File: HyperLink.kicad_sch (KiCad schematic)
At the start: 45 parts, among them J1 USB_C_Receptacle_USB2.0, J2 Conn_02x05_Odd_Even, J3 Conn_02x05_Odd_Even, SW1 SW_Push, U1 ESP32-C3, U2 PESD2USB5UXT, U3 MIC5504-3.3YM5, Y1 ABM11W-40.0000MHZ-8-B1U-T3

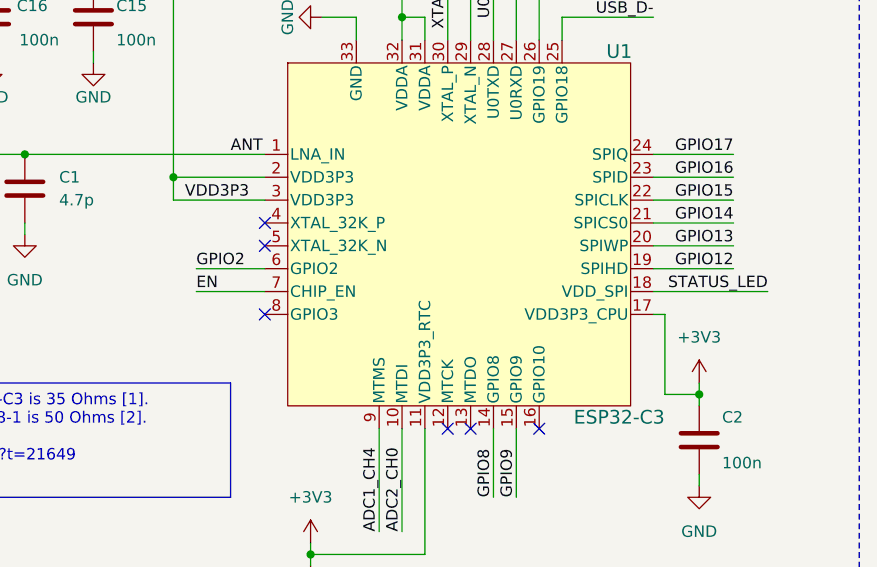
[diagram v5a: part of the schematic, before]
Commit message: Move status LED
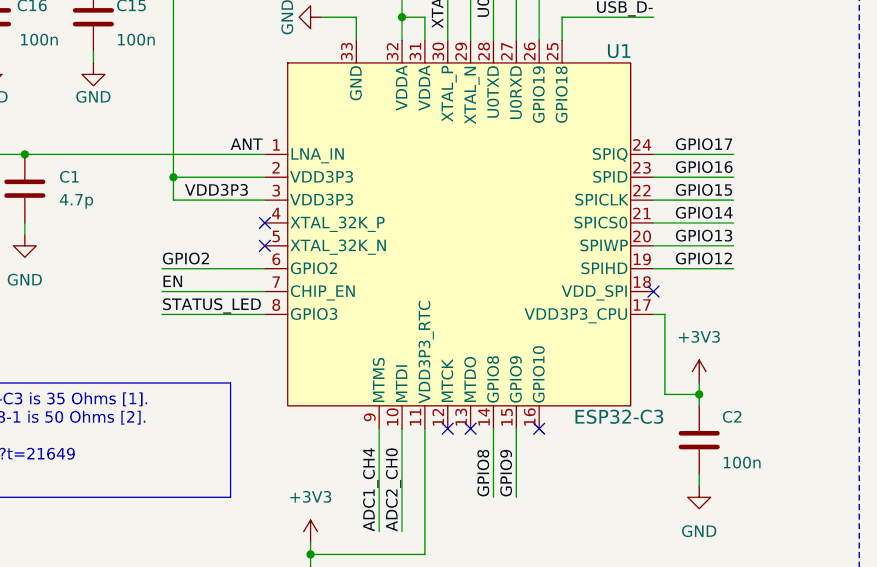
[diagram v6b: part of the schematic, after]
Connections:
- net STATUS_LED: now also U1.8 (GPIO3); no longer U1.18 (VDD_SPI)
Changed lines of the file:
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@@
   )
   (no_connect (at 241.3 116.84))
-  (no_connect (at 210.82 104.14))
   (no_connect (at 210.82 93.98))
   (no_connect (at 52.07 143.51))
   (no_connect (at 231.14 116.84))
+  (no_connect (at 254 101.6))
   (no_connect (at 52.07 146.05))
   (no_connect (at 233.68 116.84))
@@
     (stroke (width 0) (type default))
   )
-  (wire (pts (xy 203.2 99.06) (xy 210.82 99.06))
+  (wire (pts (xy 199.39 99.06) (xy 210.82 99.06))
     (stroke (width 0) (type default))
   )
@@
     (stroke (width 0) (type default))
   )
-  (wire (pts (xy 203.2 101.6) (xy 210.82 101.6))
+  (wire (pts (xy 199.39 101.6) (xy 210.82 101.6))
     (stroke (width 0) (type default))
   )
@@
     (stroke (width 0) (type default))
   )
+  (wire (pts (xy 199.39 104.14) (xy 210.82 104.14))
+    (stroke (width 0) (type default))
+  )
   (wire (pts (xy 160.02 86.36) (xy 166.37 86.36))
-    (stroke (width 0) (type default))
-  )
-  (wire (pts (xy 254 101.6) (xy 266.7 101.6))
     (stroke (width 0) (type default))
   )
@@
     (effects (font (size 1.27 1.27)) (justify left bottom))
   )
-  (label "EN" (at 203.2 101.6 0) (fields_autoplaced)
+  (label "EN" (at 199.39 101.6 0) (fields_autoplaced)
     (effects (font (size 1.27 1.27)) (justify left bottom))
   )
@@
     (effects (font (size 1.27 1.27)) (justify right bottom))
   )
+  (label "STATUS_LED" (at 199.39 104.14 0) (fields_autoplaced)
+    (effects (font (size 1.27 1.27)) (justify left bottom))
+  )
   (label "GPIO9" (at 238.76 124.46 90) (fields_autoplaced)
     (effects (font (size 1.27 1.27)) (justify left bottom))
   )
-  (label "STATUS_LED" (at 266.7 101.6 180) (fields_autoplaced)
-    (effects (font (size 1.27 1.27)) (justify right bottom))
-  )
   (label "GPIO17" (at 262.89 86.36 180) (fields_autoplaced)
     (effects (font (size 1.27 1.27)) (justify right bottom))
@@
     (effects (font (size 1.27 1.27)) (justify right bottom))
   )
-  (label "GPIO2" (at 203.2 99.06 0) (fields_autoplaced)
-    (effects (font (size 1.27 1.27)) (justify left bottom))
-  )
+  (label "GPIO2" (at 199.39 99.06 0) (fields_autoplaced)
+    (effects (font (size 1.27 1.27)) (justify left bottom))
+  )

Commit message: Check out new version of library and replace usb connector footprint
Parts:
- J1: footprint Connector_USB:USB_C_Receptacle_GCT_USB4105-xx-A_16P_TopMnt_Horizontal -> encyclopedia_galactica:USB4105-GF-A
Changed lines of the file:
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@@
       (effects (font (size 1.27 1.27)))
     )
-    (property "Footprint" "Connector_USB:USB_C_Receptacle_GCT_USB4105-xx-A_16P_TopMnt_Horizontal" (at 40.64 130.81 0)
+    (property "Footprint" "encyclopedia_galactica:USB4105-GF-A" (at 40.64 130.81 0)
       (effects (font (size 1.27 1.27)) hide)
     )

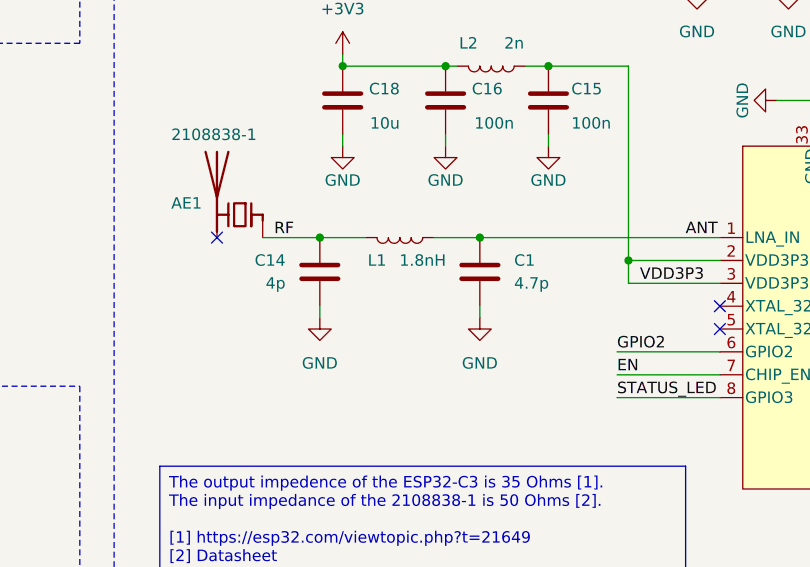
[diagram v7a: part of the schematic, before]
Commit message: Change cap values
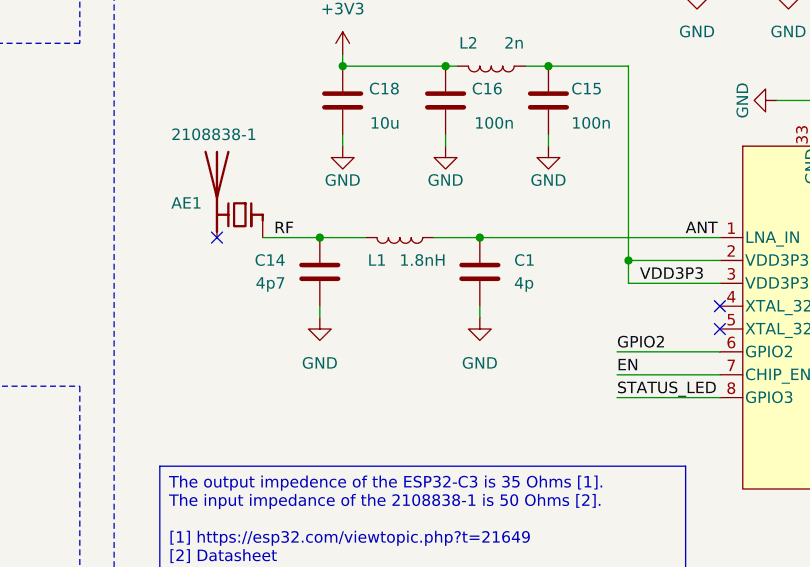
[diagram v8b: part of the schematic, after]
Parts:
- C1: value 4.7p -> 4p
- C14: value 4p -> 4p7
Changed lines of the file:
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@@
       (effects (font (size 1.27 1.27)) (justify right))
     )
-    (property "Value" "4p" (at 162.56 91.44 0)
+    (property "Value" "4p7" (at 162.56 91.44 0)
       (effects (font (size 1.27 1.27)) (justify right))
     )
@@
       (effects (font (size 1.27 1.27)) (justify right))
     )
-    (property "Value" "4.7p" (at 187.96 91.44 0)
-      (effects (font (size 1.27 1.27)) (justify right))
-    )
+    (property "Value" "4p" (at 187.96 91.44 0)
+      (effects (font (size 1.27 1.27)) (justify right))
+    )
